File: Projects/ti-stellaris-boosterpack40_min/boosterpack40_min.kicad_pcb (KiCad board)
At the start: 2 copper layers, 50.8 x 34.3 mm, 4 parts, among them J1 TI_BOOSTER_40_J1, J2 TI_BOOSTER_40_J2, J3 TI_BOOSTER_40_J3, J4 TI_BOOSTER_40_J4

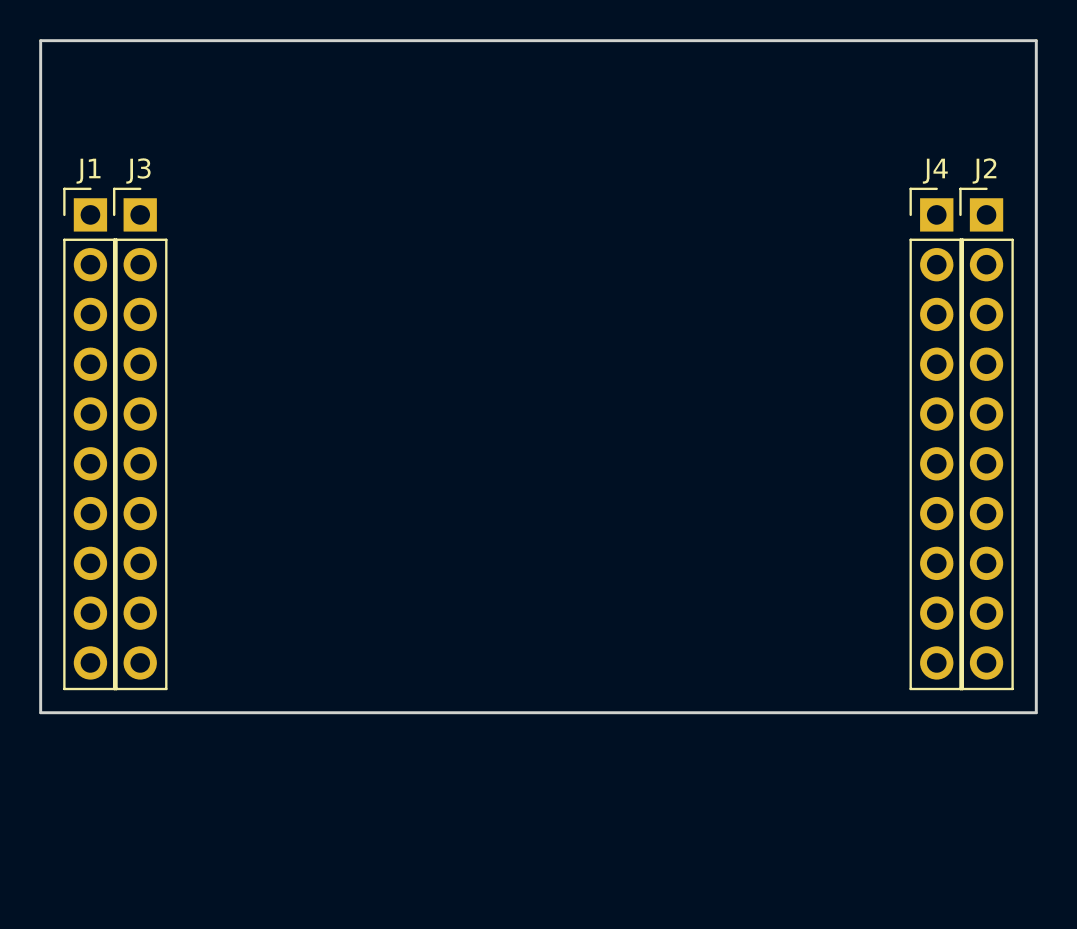
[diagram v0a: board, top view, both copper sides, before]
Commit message: Update ti-stellaris-boosterpack40 with KiCad 5.1.6
* Repointed all symbols and footprints to current libraries.
* Updated header pinouts to match TI documentation.
* Updated documentation.
* Derived new template for 20-pin BoosterPack.
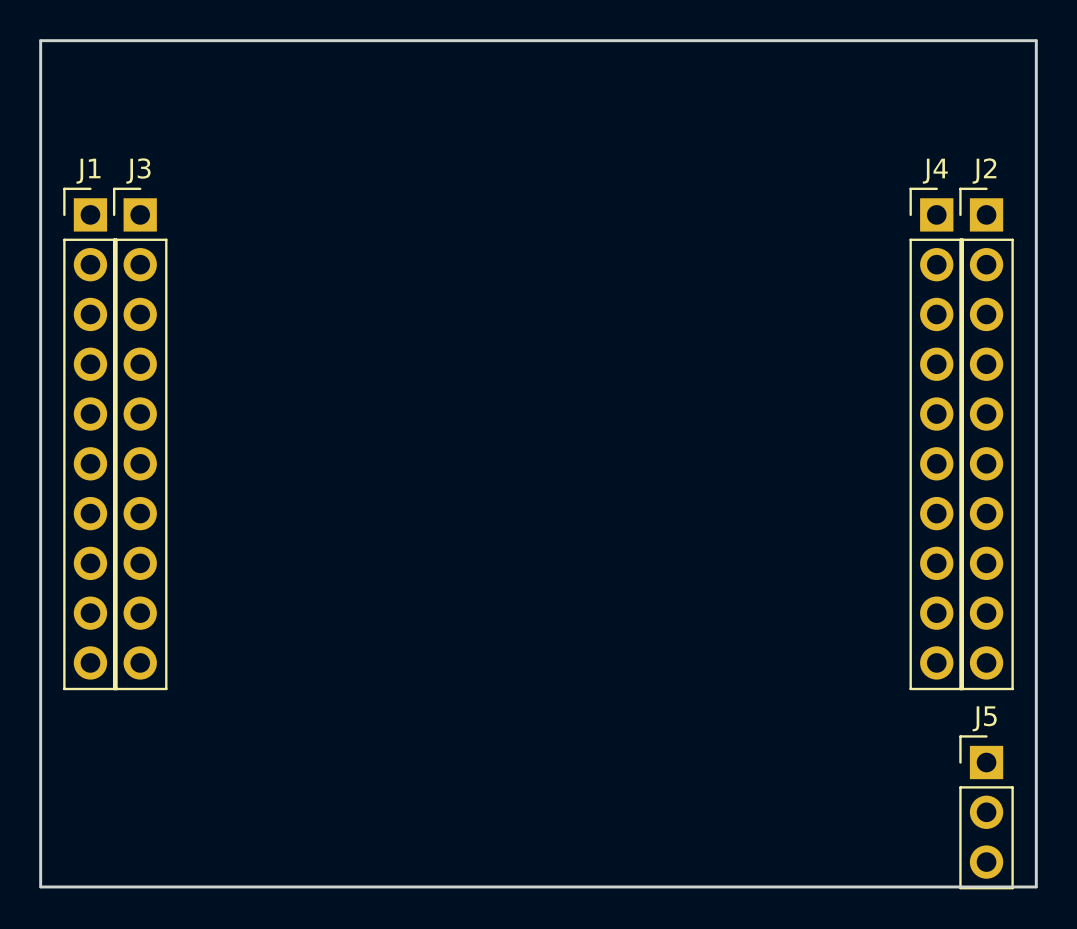
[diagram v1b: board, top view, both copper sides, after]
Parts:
- added J5: Conn_01x03, Connector_PinHeader_2.54mm:PinHeader_1x03_P2.54mm_Vertical, F.Cu at (231.1, 149.9)
- J1: value TI_BOOSTER_40_J1 -> Ti_Booster_40_J1
- J2: value TI_BOOSTER_40_J2 -> Ti_Booster_40_J2
- J3: value TI_BOOSTER_40_J3 -> Ti_Booster_40_J3
- J4: value TI_BOOSTER_40_J4 -> Ti_Booster_40_J4
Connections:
- J1 pad 10: Net-(J1-Pad10) -> (no net)
- J1 pad 2: Net-(J1-Pad2) -> (no net)
- J1 pad 3: Net-(J1-Pad3) -> (no net)
- J1 pad 4: Net-(J1-Pad4) -> (no net)
- J1 pad 5: Net-(J1-Pad5) -> (no net)
- J1 pad 6: Net-(J1-Pad6) -> (no net)
- J1 pad 7: Net-(J1-Pad7) -> (no net)
- J1 pad 8: Net-(J1-Pad8) -> (no net)
- J1 pad 9: Net-(J1-Pad9) -> (no net)
- J2 pad 10: Net-(J2-Pad10) -> (no net)
- J2 pad 2: Net-(J2-Pad2) -> (no net)
- J2 pad 3: Net-(J2-Pad3) -> (no net)
- J2 pad 4: Net-(J2-Pad4) -> (no net)
- J2 pad 5: Net-(J2-Pad5) -> (no net)
- J2 pad 6: Net-(J2-Pad6) -> (no net)
- J2 pad 7: Net-(J2-Pad7) -> (no net)
- J2 pad 8: Net-(J2-Pad8) -> (no net)
- J2 pad 9: Net-(J2-Pad9) -> (no net)
- J3 pad 1: +5V -> (no net)
- J3 pad 10: Net-(J3-Pad10) -> (no net)
- J3 pad 3: Net-(J3-Pad3) -> (no net)
- J3 pad 4: Net-(J3-Pad4) -> (no net)
- J3 pad 5: Net-(J3-Pad5) -> (no net)
- J3 pad 6: Net-(J3-Pad6) -> (no net)
- J3 pad 7: Net-(J3-Pad7) -> (no net)
- J3 pad 8: Net-(J3-Pad8) -> (no net)
- J3 pad 9: Net-(J3-Pad9) -> (no net)
- J4 pad 1: Net-(J4-Pad1) -> (no net)
- J4 pad 10: Net-(J4-Pad10) -> (no net)
- J4 pad 2: Net-(J4-Pad2) -> (no net)
- J4 pad 3: Net-(J4-Pad3) -> (no net)
- J4 pad 4: Net-(J4-Pad4) -> (no net)
- J4 pad 5: Net-(J4-Pad5) -> (no net)
- J4 pad 6: Net-(J4-Pad6) -> (no net)
- J4 pad 7: Net-(J4-Pad7) -> (no net)
- J4 pad 8: Net-(J4-Pad8) -> (no net)
- J4 pad 9: Net-(J4-Pad9) -> (no net)
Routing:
- added copper zone on B.Cu, net GND
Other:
- board size 50.8 x 34.3 mm -> 50.8 x 43.2 mm
